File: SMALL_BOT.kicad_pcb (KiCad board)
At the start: 2 copper layers, 80 x 65 mm, 22 parts, among them J1 MOTOR_B, J10 HEADER_2, J11 Conn_01x04, J2 MOTOR_A, J3 HEADER_2, J4 HEADER_2, J5 Conn_01x04, J6 Conn_01x04, J7 Conn_01x04, J8 Conn_01x04, J9 HEADER_2, Q1 2N7002, U1 Teensy4.0, U2 DRV8833_POLOLU, U3 LM1117-SOT

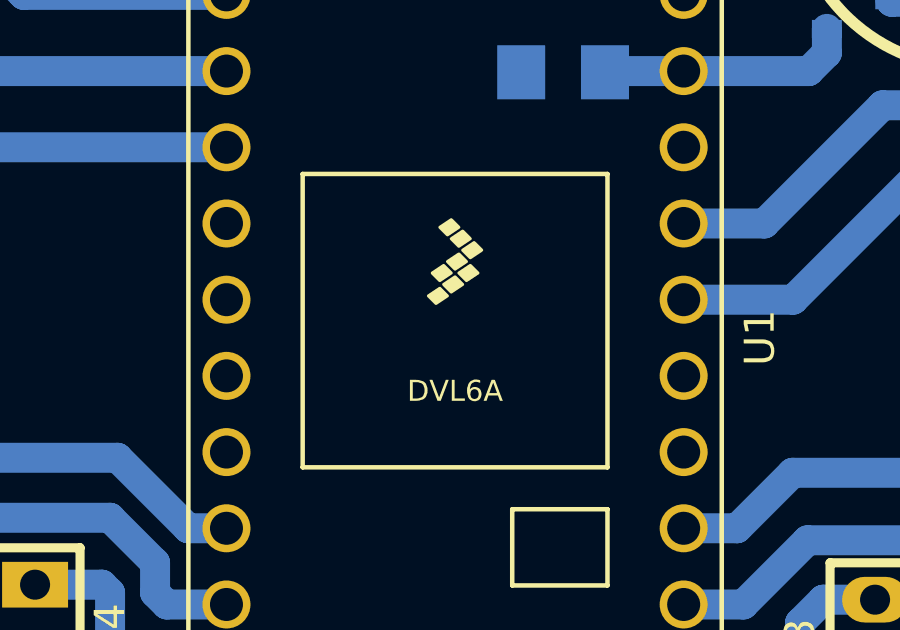
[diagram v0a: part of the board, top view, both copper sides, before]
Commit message: logo
se agrego un logo al pcb
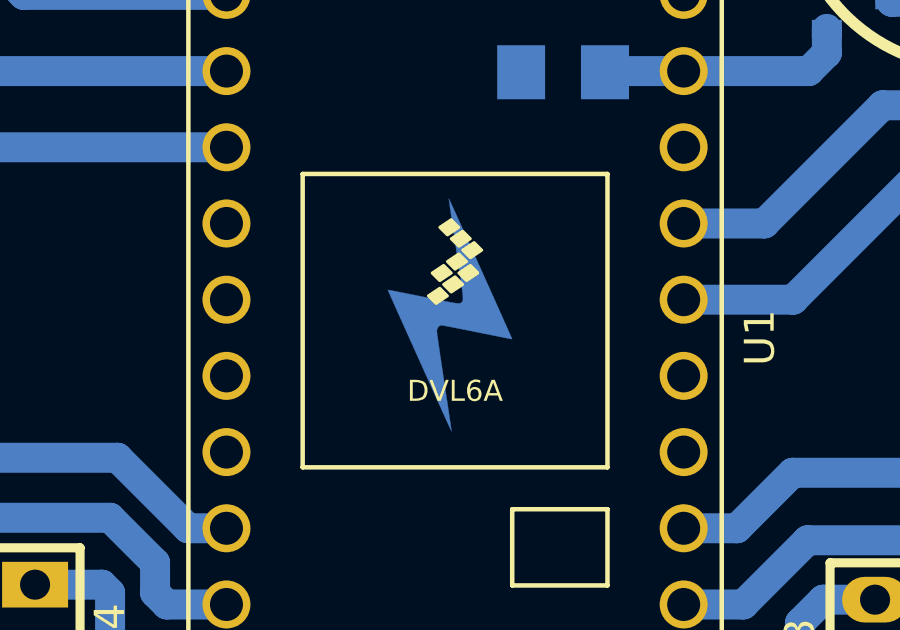
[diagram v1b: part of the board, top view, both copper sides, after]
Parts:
- added G***: LOGO, EESTN5:Logo_Rayo, F.Cu at (120.1, 106.7)

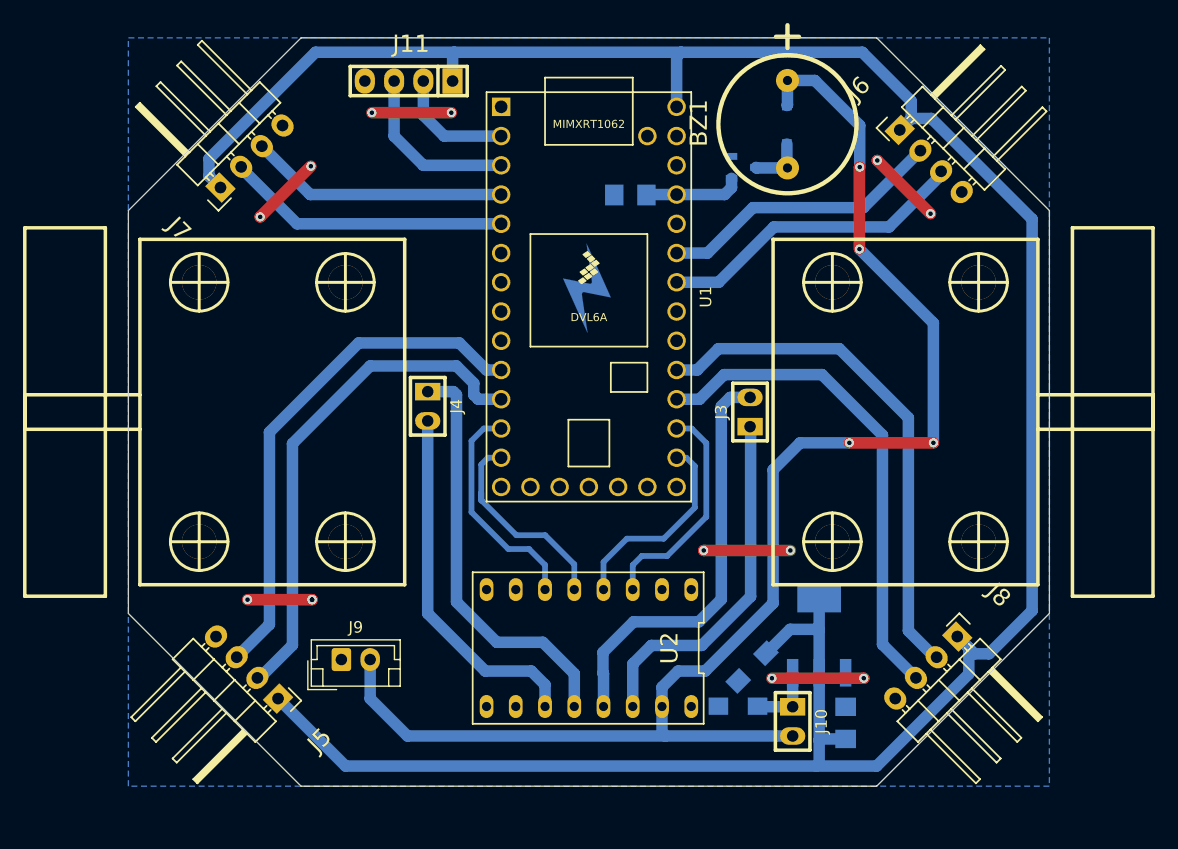
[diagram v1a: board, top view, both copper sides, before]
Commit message: se modifico pcb
se movieron de lugar los conectores para los sensores ultrasonidos y se agrego pantalla oled
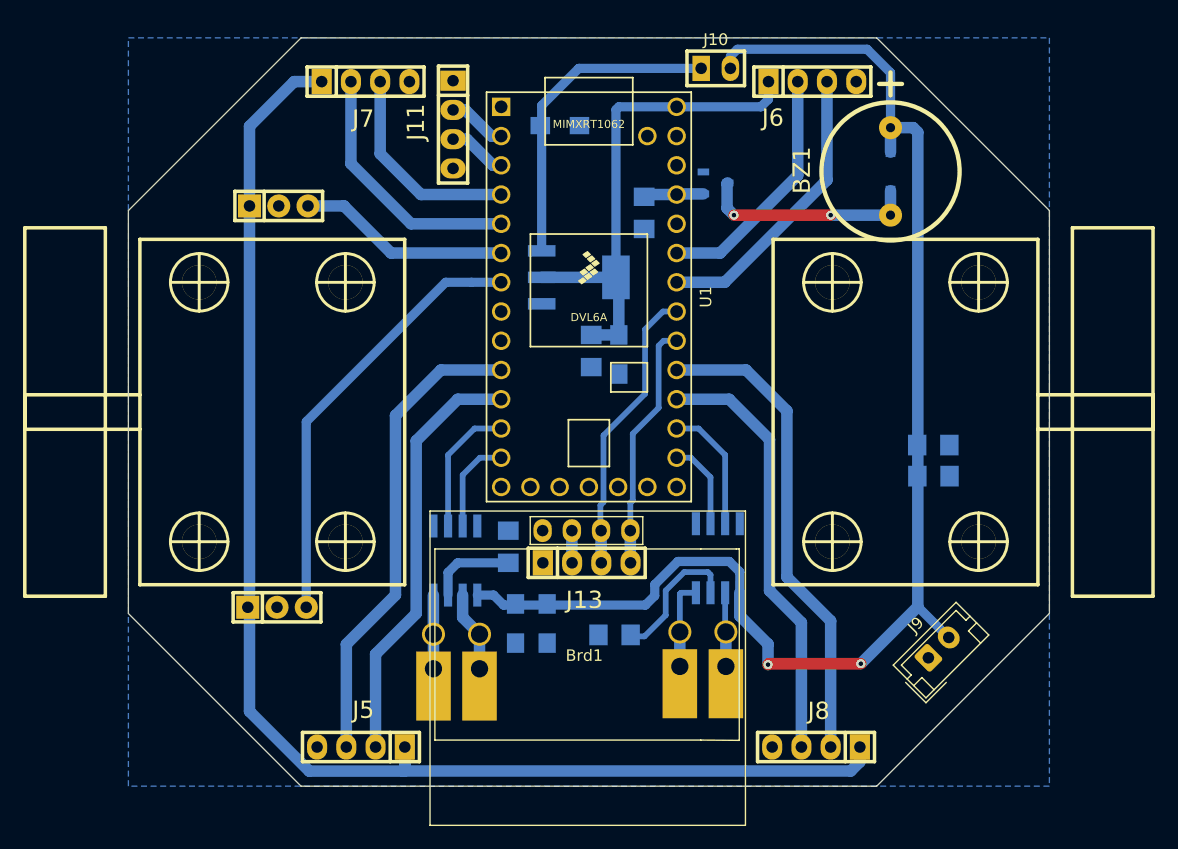
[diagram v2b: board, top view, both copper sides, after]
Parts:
- removed G***: LOGO, EESTN5:Logo_Rayo
- added Brd1: SSD1306, SSD1306:128x64OLED, F.Cu at (119.6, 138.4)
- added C4: C, EESTN5:C_1206, B.Cu at (149.9, 123.1)
- added C5: CAPAPOL, EESTN5:CAP_TAN_A, B.Cu at (113.6, 135.9)
- added C6: C, EESTN5:C_1206, B.Cu at (149.9, 120.4)
- added C7: CAPAPOL, EESTN5:CAP_TAN_A, B.Cu at (116.4, 135.9)
- added J12: LEDS, EESTN5:Pin_Strip_3, F.Cu at (93.1, 99.6)
- added J13: I2C, EESTN5:pin_strip_4, F.Cu at (119.8, 130.6)
- added J14: LEDS, EESTN5:Pin_Strip_3, F.Cu at (92.9, 134.5)
- added J15: HEADER_1, EESTN5:Cable_Doble_1,5mm, F.Cu at (127.9, 139.6)
- added J16: HEADER_1, EESTN5:Cable_Doble_1,5mm, F.Cu at (131.9, 139.6)
- added R2: R, EESTN5:R_1206, B.Cu at (113.0, 129.2)
- added R3: R, EESTN5:R_1206, B.Cu at (122.2, 136.9)
- added U4: DRV8872, EESTN5:SSOP-8, B.Cu at (131.2, 130.2)
- J3, J4: value HEADER_2 -> HEADER_1; footprint EESTN5:Pin_strip_2 -> EESTN5:Cable_Doble_1,5mm
- J5, J6, J7, J8: value Conn_01x04 -> ULTRASONICO; footprint EESTN5:HEADER-4H -> EESTN5:pin_strip_4
- U2: value DRV8833_POLOLU -> DRV8872; footprint EESTN5:DRV8833_Pololu -> EESTN5:SSOP-8; moved to B.Cu
- moved J10 57.1 mm to (131.0, 87.7), turned to 0 degrees
- moved C1 52.7 mm to (117.5, 92.6), turned to 0 degrees
- moved J9 51.0 mm to (149.5, 138.8), turned to 45 degrees
- moved C2 39.1 mm to (120.2, 112.2), turned to 90 degrees
- moved U3 37.4 mm to (119.2, 105.8), turned to 90 degrees
- moved J3 35.4 mm to (106.5, 139.8), turned to 0 degrees
- moved C3 29.5 mm to (122.6, 112.5), turned to 270 degrees
- moved J4 23.2 mm to (110.5, 139.8), turned to 0 degrees
- moved J7 15.6 mm to (100.6, 88.8), turned to 0 degrees
- moved J8 15.6 mm to (139.7, 146.6), turned to 180 degrees
- moved U2 13.9 mm to (108.4, 130.4), turned to 0 degrees
- moved D1 9.87 mm to (146.2, 96.6)
- moved BZ1 9.84 mm to (146.2, 96.6)
- moved J6 8.67 mm to (139.4, 88.8), turned to 0 degrees
- moved J5 8.34 mm to (100.2, 146.6), turned to 180 degrees
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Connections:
- J1 pad 1: Net-(J1-Pad1) -> (no net)
- J1 pad 2: Net-(J1-Pad2) -> (no net)
- J2 pad 1: Net-(J2-Pad1) -> (no net)
- J2 pad 2: Net-(J2-Pad2) -> (no net)
- U1 pad 14: Net-(U1-Pad14) -> (no net)
- U1 pad 15: Net-(U1-Pad15) -> (no net)
- U1 pad 16: Net-(U1-Pad16) -> (no net)
- U1 pad 18: Net-(U1-Pad18) -> (no net)
- U1 pad 19: Net-(U1-Pad19) -> (no net)
- U1 pad 20: Net-(U1-Pad20) -> (no net)
- U1 pad 25: Net-(U1-Pad25) -> /SDA
- U1 pad 26: Net-(U1-Pad26) -> /SCL
- U1 pad 29: Net-(U1-Pad29) -> (no net)
- U1 pad 31: Net-(U1-Pad31) -> (no net)
- U1 pad 34: Net-(U1-Pad34) -> (no net)
- U1 pad 6: Net-(U1-Pad6) -> /NEOPIXEL
- U1 pad 7: Net-(U1-Pad7) -> /NEOPIXEL1
- U1 pad 8: Net-(U1-Pad8) -> (no net)
- U1 pad 9: Net-(U1-Pad9) -> (no net)
- U2 pad 2: Net-(U2-Pad2) -> /M1B
- U2 pad 3: /M2A -> /M1A
- U2 pad 4: /M2B -> (no net)
- U2 pad 5: /M1A -> /VIN
- U2 pad 6: /M1B -> Net-(J4-Pad1)
- U2 pad 8: Net-(U2-Pad8) -> Net-(J3-Pad1)
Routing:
- net +5V: track 228.3 -> 166.0 mm
- net GND: track 40.8 -> 0.00 mm, vias 13 -> 0
- net /NEOPIXEL1: track 0.00 -> 38.1 mm
- net Net-(J3-Pad2): track 36.5 -> 0.00 mm
- net Net-(J4-Pad2): track 31.4 -> 0.00 mm
- net Net-(J4-Pad1): track 36.3 -> 7.01 mm
- net /SCL: track 0.00 -> 25.5 mm
- net Net-(J3-Pad1): track 30.6 -> 6.40 mm
- net Net-(C1-Pad1): track 6.02 -> 27.8 mm
- net /SDA: track 0.00 -> 21.7 mm
- net /NEOPIXEL: track 0.00 -> 18.5 mm
- net Net-(BZ1-Pad2): track 4.86 -> 18.8 mm, vias 0 -> 2
- net Net-(R3-Pad1): track 0.00 -> 12.3 mm
- net /M2B: track 17.8 -> 7.68 mm
- net /RX: track 15.1 -> 5.12 mm
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
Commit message: Varios
Falta verificar al 100% la compatibilidad con los 3.3v para la Teensy.
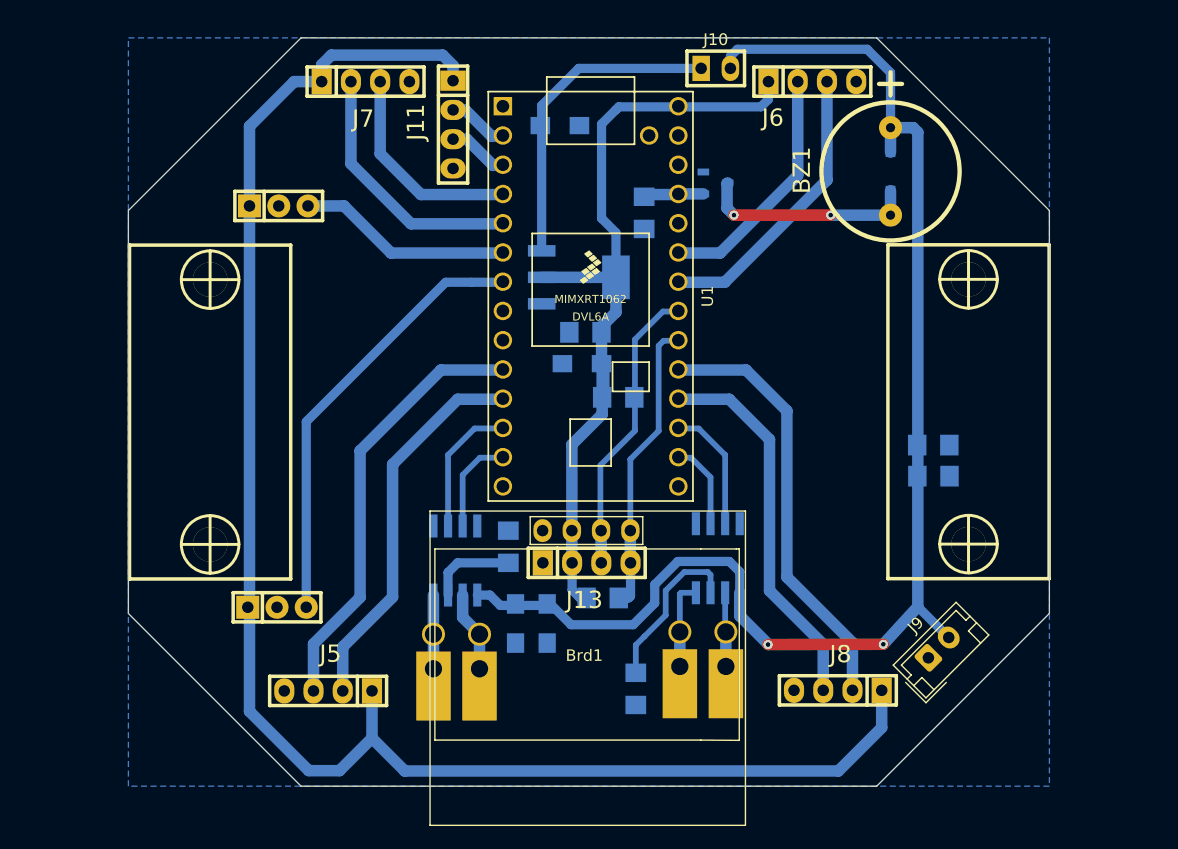
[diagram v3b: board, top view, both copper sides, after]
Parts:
- added R4: 10k, EESTN5:R_1206, B.Cu at (121.2, 133.7)
- added R5: 10k, EESTN5:R_1206, B.Cu at (122.5, 116.2)
- C1: value CAPAPOL -> 1000uf
- C2, C4: value C -> 100nf
- C3: value CAPAPOL -> 10uf
- C5: value CAPAPOL -> 100uf
- C6: value C -> 100nF
- C7: value CAPAPOL -> 100uF
- J1, J2: footprint EESTN5:Pololu_Micro_Gear_Motor_W_Mount -> EESTN5:Pololu_Micro_Con_Soporte_Simple
- J10: value HEADER_2 -> JMP
- J11: value Conn_01x04 -> UART
- J5, J6, J7, J8: value ULTRASONICO -> HC-SR04
- J9: value HEADER_2 -> Bateria
- R1: value R -> 10k
- R2, R3: value R -> 0,25
- U1: value Teensy4.0 -> Teensy4.0_B; footprint EESTN5:Teensy40 -> EESTN5:Teensy40_B
- moved J5 5.65 mm to (97.3, 141.7)
- moved J1 5.48 mm to (153.0, 117.5)
- moved J2 5.40 mm to (87.1, 117.5)
- moved J8 5.28 mm to (141.6, 141.7)
- moved R3 5.04 mm to (124.1, 141.6), turned to 90 degrees
- moved C3 3.30 mm to (119.4, 113.3), turned to 180 degrees
- moved C2 1.70 mm to (119.7, 110.6), turned to 0 degrees
- moved U1 0.16 mm to (120.2, 107.5)
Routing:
- net +5V: track 166.0 -> 211.7 mm
- net /ECHO3: track 37.4 -> 33.2 mm
- net /TRIG3: track 41.8 -> 37.7 mm
- net /SDA: track 21.7 -> 25.6 mm
- net /TRIG0: track 36.9 -> 33.2 mm
- net /ECHO0: track 41.4 -> 37.7 mm
- net Net-(R3-Pad1): track 12.3 -> 14.4 mm
- net /VIN: track 120.6 -> 122.7 mm

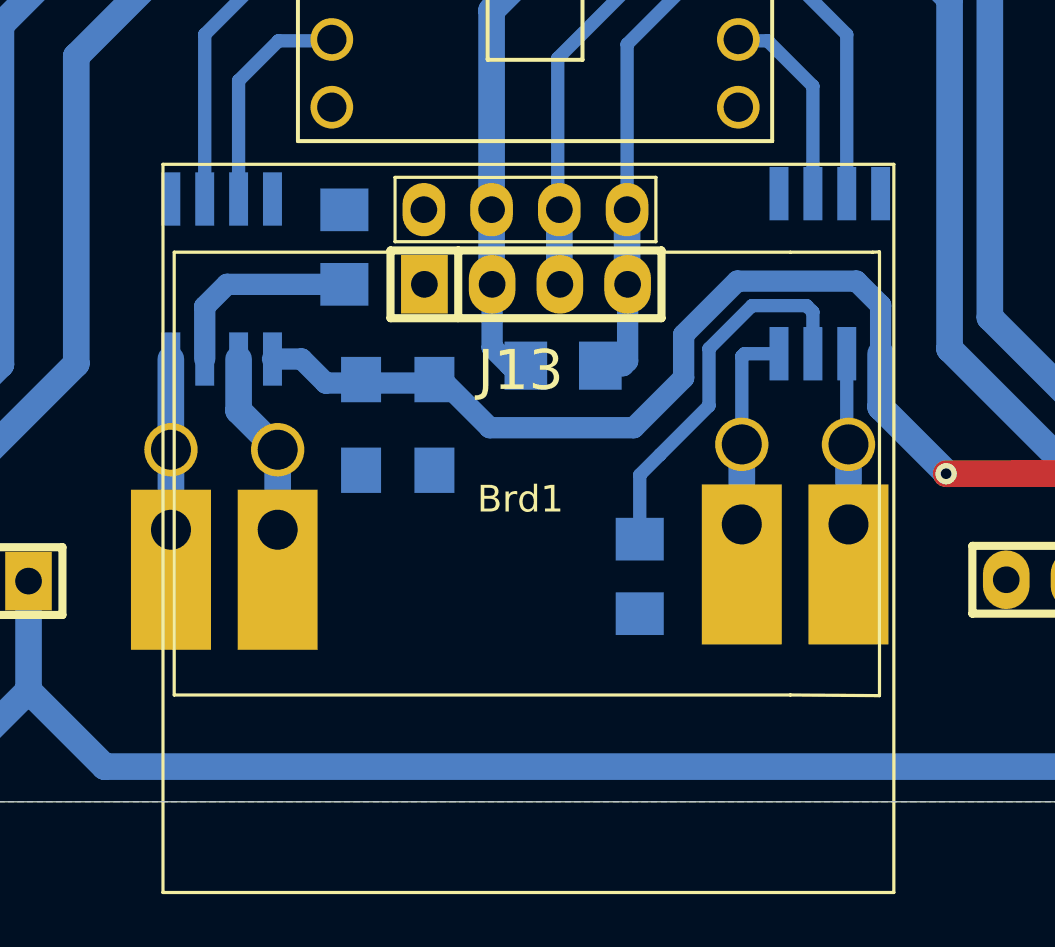
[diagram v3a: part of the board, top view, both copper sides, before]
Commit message: Pantalla Oled
Actualice la pantalla oled
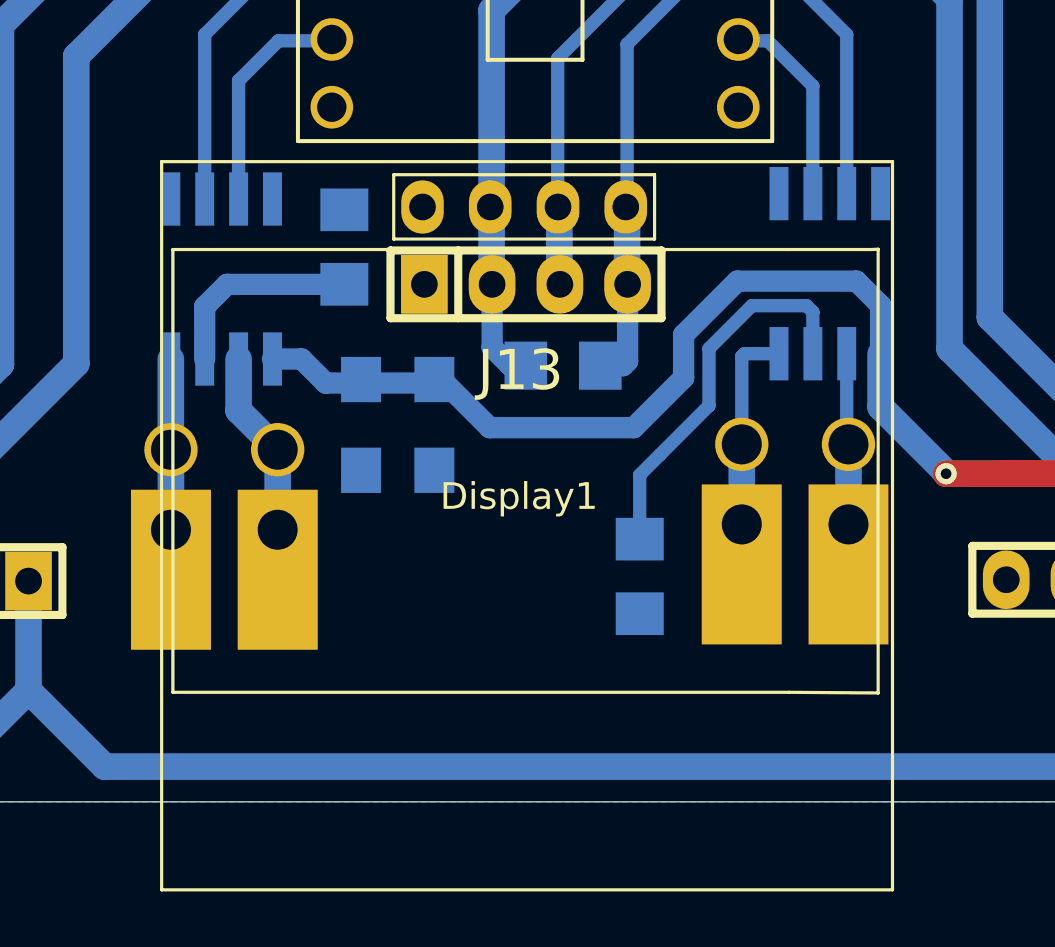
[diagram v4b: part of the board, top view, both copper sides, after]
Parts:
- removed Brd1: SSD1306, SSD1306:128x64OLED
- added Display1: SSD1306-SSD1306-128x64_OLED, EESTN5:128x64OLED, F.Cu at (119.5, 138.3)
